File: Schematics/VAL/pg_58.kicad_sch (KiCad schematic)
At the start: 16 parts, among them U6001 F194, U6002 F194, U6003 F194, U6004 F194, U6005 F194, U6006 F194, U6007 F04, U6008 F138, U6009 F138, U6010 F37, U6011 F37, U6012 F240, U6013 F08, U6014 F00, U6015 F00, U6016 F00

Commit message: Align to grid
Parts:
- removed U6001, U6002, U6003, U6004, U6005, U6006: F194, symbol r1000:F194
- removed U6007: F04, symbol r1000:F04
- removed U6008, U6009: F138, symbol r1000:F138
- removed U6010, U6011: F37, symbol r1000:F37
- removed U6012: F240, symbol r1000:F240
- removed U6013: F08, symbol r1000:F08
- removed U6014, U6015, U6016: F00, symbol r1000:F00
- added U (x2): (no value), symbol r1000:F138
- added U (x3): (no value), symbol r1000:F00
- added U (x6): (no value), symbol r1000:F194
- added U: (no value), symbol r1000:F08
- added U (x2): (no value), symbol r1000:F37
- added U: (no value), symbol r1000:F240
- added U: (no value), symbol r1000:F04
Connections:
- net ALU_RAND0: now also U.3 (Q)
- net ALU_RAND1: now also U.3 (Q)
- net ALU_RAND2: now also U.3 (Q)
- net COND_TO_FIU~: now also U.1 (D0), U.12 (Y3_)
- net COUNT_ZEROS~: now also U.10 (Y5_)
- net C_MUX.SEL0: now also U.15 (Q0)
- net C_MUX.SEL1: now also U.1 (D0), U.14 (Q1)
- net C_MUX.SEL1.B0: now also U.3 (Q)
- net C_MUX.SEL1.B1: now also U.3 (Q)
- net DEC_LOOP~: now also U.13 (Y2_)
- net DIAG.D10: now also U.14 (Y2)
- net DIAG.D11: now also U.12 (Y3), U.2 (RSI)
- net DIAG.D12: now also U.2 (RSI), U.9 (Y4)
- net DIAG.D8: now also U.18 (Y0)
- net DIAG.D9: now also U.16 (Y1)
- net DIVIDE~: now also U.12 (Y3_)
- net FORCE_PASS_A~: now also U.1 (CLR), U.1 (CLR), U.1 (CLR), U.1 (D0), U.2 (D1)
- net FRAME~3: now also U.4 (I1)
- net GET_LIT~: now also U.2 (D1), U.9 (Y6_)
- net INC_LOOP~: now also U.14 (Y1_)
- net PD: now also U.4 (D1), U.5 (D2), U.5 (D2)
- net PROD_LEFT_16~: now also U.10 (Y5_)
- net PROD_LEFT_32~: now also U.9 (Y6_)
- net PU: now also U.1 (CLR), U.1 (CLR), U.1 (CLR), U.13 (I5), U.15 (I6), U.17 (I7), U.6 (D0), U.9 (S0), U.9 (S0), U.9 (S0), U.9 (S0), U.9 (S0), U.9 (S0)
- net SCAN_UIR~: now also U.1 (OE0), U.19 (OE1)
- net SNEAK.EN~: now also U.3 (Q)
- net SPLIT_C_SRC~: now also U.11 (Y4_)
- net START_MULT~: now also U.11 (Y4_)
- net UIR.ALU_FUNC0: now also U.13 (Q2)
- net UIR.ALU_FUNC1: now also U.12 (Q3), U.2 (RSI)
- net UIR.ALU_FUNC2: now also U.15 (Q0)
- net UIR.ALU_FUNC3: now also U.14 (Q1)
- net UIR.ALU_FUNC4: now also U.13 (Q2)
- net UIR.B~1: now also U.2 (I0)
- net UIR.C0: now also U.15 (Q0)
- net UIR.C1: now also U.14 (Q1)
- net UIR.C2: now also U.13 (Q2)
- net UIR.C3: now also U.12 (Q3), U.2 (RSI)
- net UIR.C4: now also U.15 (Q0)
- net UIR.C5: now also U.14 (Q1)
- net UIR.C_SOURCE: now also U.11 (I4), U.12 (Q3)
- net UIR.FRAME4: now also U.2 (RSI)
- net UIR.M_A_SRC0: now also U.13 (Q2)
- net UIR.M_A_SRC1: now also U.12 (Q3), U.8 (I3)
- net UIR.M_B_SRC0: now also U.15 (Q0)
- net UIR.M_B_SRC1: now also U.14 (Q1)
- net UIR.P: now also U.13 (Q2), U.2 (RSI)
- net UIR.RAND0: now also U.1 (D0), U.15 (Q0), U.2 (D1), U.2 (D1), U.4 (D1), U.6 (D0)
- net UIR.RAND1: now also U.1 (D0), U.14 (Q1), U.3 (S0), U.3 (S0)
- net UIR.RAND2: now also U.1 (D0), U.13 (Q2), U.2 (S1), U.2 (S1)
- net UIR.RAND3: now also U.1 (S2), U.1 (S2), U.12 (Q3), U.2 (D1), U.6 (I2)
- net UIR.SEL0: now also U.10 (S1), U.10 (S1), U.10 (S1), U.10 (S1), U.10 (S1), U.10 (S1)
- net UIR~.SCLK.B1: now also U.11 (CLK), U.11 (CLK), U.11 (CLK), U.11 (CLK)
- net UIR~.SCLK.B2: now also U.11 (CLK), U.11 (CLK)
- net WCS.D17: now also U.3 (D0)
- net WCS.D18: now also U.4 (D1)
- net WCS.D19: now also U.3 (D0)
- net WCS.D20: now also U.4 (D1)
- net WCS.D21: now also U.5 (D2)
- net WCS.D22: now also U.6 (D3)
- net WCS.D23: now also U.3 (D0)
- net WCS.D24: now also U.4 (D1)
- net WCS.D25: now also U.5 (D2)
- net WCS.D26: now also U.6 (D3)
- net WCS.D27: now also U.3 (D0)
- net WCS.D28: now also U.4 (D1)
- net WCS.D29: now also U.5 (D2)
- net WCS.D30: now also U.6 (D3)
- net WCS.D31: now also U.3 (D0)
- net WCS.D32: now also U.4 (D1)
- net WCS.D33: now also U.5 (D2)
- net WCS.D34: now also U.6 (D3)
- net WCS.D35: now also U.3 (D0)
- net WCS.D36: now also U.4 (D1)
- net WCS.D37: now also U.5 (D2)
- net WCS.D38: now also U.6 (D3)
- net WCS.P: now also U.5 (D2)
- new net: U.1 (D0), U.2 (D1), U.2 (Q)

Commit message: VAL: dedup, clock, dfsm
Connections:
- net UIR~.SCLK.B2 is gone; now on net UIR~.SCLK: U.11 (CLK), U.11 (CLK)
- net UIR~.SCLK.B1 renamed UIR~.SCLK
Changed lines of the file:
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@@
     )
   )
-  (global_label "UIR~.SCLK.B1" (shape input) (at 55.88 27.94 180) (fields_autoplaced)
+  (global_label "UIR~.SCLK" (shape input) (at 55.88 27.94 180) (fields_autoplaced)
     (effects (font (size 2.54 2.54)) (justify right))
     (property "Intersheet References" "${INTERSHEET_REFS}" (id 0) (at 25.8959 27.7813 0)
@@
     )
   )
-  (global_label "UIR~.SCLK.B2" (shape input) (at 309.88 22.86 180) (fields_autoplaced)
+  (global_label "UIR~.SCLK" (shape input) (at 309.88 22.86 180) (fields_autoplaced)
     (effects (font (size 2.54 2.54)) (justify right))
     (property "Intersheet References" "${INTERSHEET_REFS}" (id 0) (at 279.8959 22.7013 0)

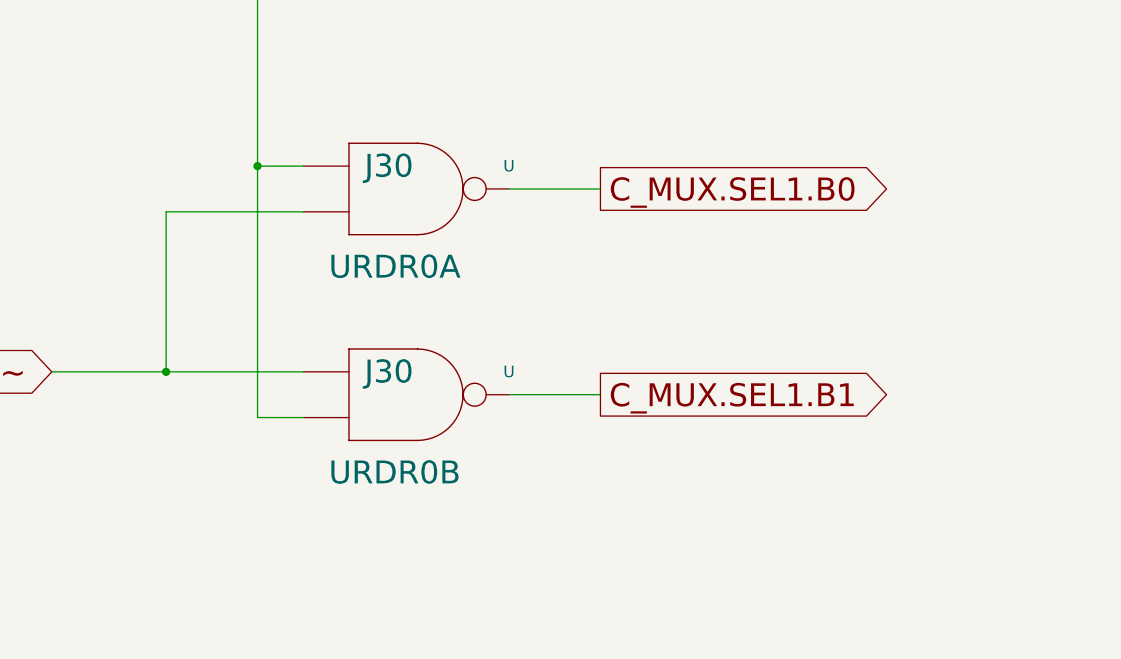
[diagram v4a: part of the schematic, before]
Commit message: VAL & SEQ: tested to 6.0 seconds (rm021)
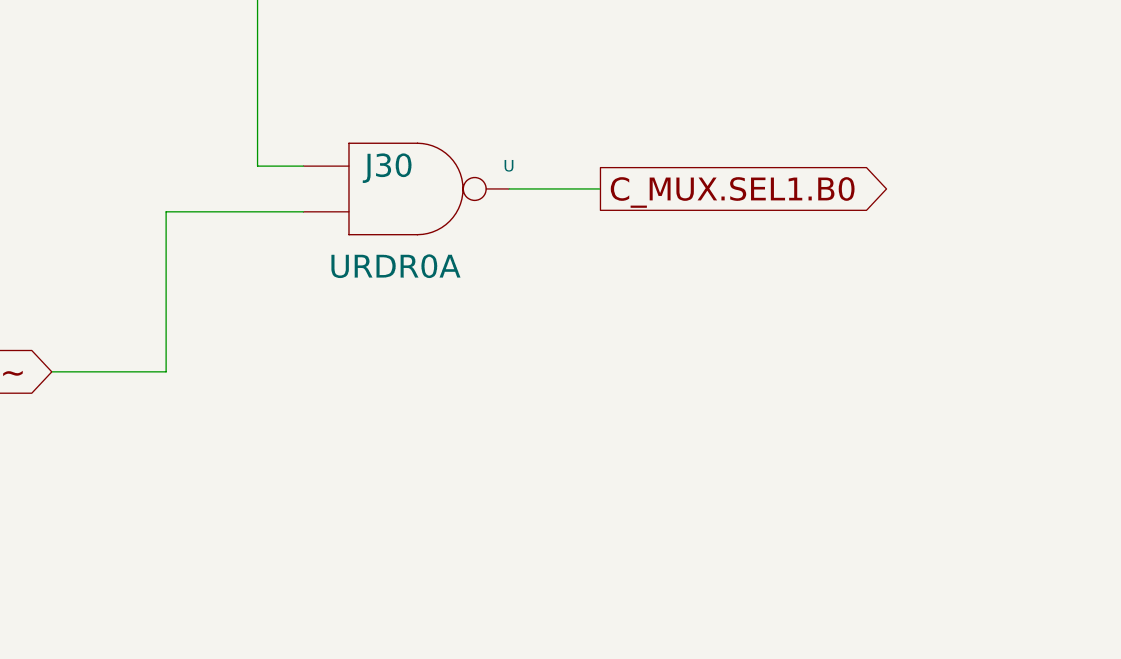
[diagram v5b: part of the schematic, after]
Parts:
- removed U: (no value), symbol r1000:F37
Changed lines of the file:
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@@
   (junction (at 325.12 109.22) (diameter 0) (color 0 0 0 0)
   )
-  (junction (at 208.28 91.44) (diameter 0) (color 0 0 0 0)
-  )
   (junction (at 490.22 208.28) (diameter 0) (color 0 0 0 0)
   )
@@
   )
   (junction (at 15.24 134.62) (diameter 0) (color 0 0 0 0)
-  )
-  (junction (at 198.12 114.3) (diameter 0) (color 0 0 0 0)
   )
   (junction (at 175.26 220.98) (diameter 0) (color 0 0 0 0)
@@
     (stroke (width 0) (type default))
   )
-  (wire (pts (xy 208.28 91.44) (xy 208.28 119.38))
-    (stroke (width 0) (type default))
-  )
   (wire (pts (xy 91.44 129.54) (xy 91.44 139.7))
     (stroke (width 0) (type default))
@@
     (stroke (width 0) (type default))
   )
-  (wire (pts (xy 236.22 116.84) (xy 246.38 116.84))
-    (stroke (width 0) (type default))
-  )
   (bus (pts (xy 25.4 81.28) (xy 25.4 157.48))
     (stroke (width 0) (type default))
@@
     (stroke (width 0) (type default))
   )
-  (wire (pts (xy 208.28 119.38) (xy 213.36 119.38))
-    (stroke (width 0) (type default))
-  )
   (wire (pts (xy 342.9 73.66) (xy 381 73.66))
     (stroke (width 0) (type default))
@@
   )
   (bus (pts (xy 25.4 238.76) (xy 25.4 243.84))
-    (stroke (width 0) (type default))
-  )
-  (wire (pts (xy 198.12 114.3) (xy 213.36 114.3))
     (stroke (width 0) (type default))
   )
@@
     (effects (font (size 2.54 2.54)) (justify left))
     (property "Intersheet References" "${INTERSHEET_REFS}" (id 0) (at 262.0917 164.9413 0)
-      (effects (font (size 1.905 1.905)) (justify left))
-    )
-  )
-  (global_label "C_MUX.SEL1.B1" (shape output) (at 246.38 116.84 0) (fields_autoplaced)
-    (effects (font (size 2.54 2.54)) (justify left))
-    (property "Intersheet References" "${INTERSHEET_REFS}" (id 0) (at 280.2346 116.6813 0)
       (effects (font (size 1.905 1.905)) (justify left))
     )
@@
     (pin "9")
   )
-  (symbol (lib_id "r1000:F37") (at 220.98 114.3 0) (unit 1)
-    (in_bom yes) (on_board yes)
-    (default_instance (reference "U") (unit 1) (value "") (footprint ""))
-    (property "Reference" "U" (id 0) (at 236.22 114.3 0)
-      (effects (font (size 1.27 1.27)))
-    )
-    (property "Value" "" (id 1) (at 222.885 119.38 0)
-      (effects (font (size 2.54 2.54)))
-    )
-    (property "Footprint" "" (id 2) (at 220.98 101.6 0)
-      (effects (font (size 1.27 1.27)) hide)
-    )
-    (property "Datasheet" "" (id 3) (at 220.98 101.6 0)
-      (effects (font (size 1.27 1.27)) hide)
-    )
-    (property "Location" "J30" (id 4) (at 222.885 114.3 0)
-      (effects (font (size 2.54 2.54)))
-    )
-    (property "Name" "URDR0B" (id 5) (at 223.52 127 0)
-      (effects (font (size 2.54 2.54)) (justify bottom))
-    )
-    (pin "1")
-    (pin "2")
-    (pin "3")
-  )
   (symbol (lib_id "r1000:F240") (at 233.68 327.66 0) (unit 1)

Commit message: Tested to 12.05s (rc016)
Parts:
- removed U (x4): (no value), symbol r1000:F194
- added U (x2): XSR8, symbol r1000:XSR8
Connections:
- net DIAG.D11: now also U.3 (RSI)
- net DIAG.D12: now also U.3 (RSI)
- net FORCE_PASS_A~: now also U.2 (CLR)
- net PU: now also U.5 (S0), U.5 (S0)
- net UIR.ALU_FUNC0: now also U.17 (Q2)
- net UIR.ALU_FUNC1: now also U.18 (Q3)
- net UIR.ALU_FUNC2: now also U.19 (Q4)
- net UIR.ALU_FUNC3: now also U.20 (Q5)
- net UIR.ALU_FUNC4: now also U.21 (Q6)
- net UIR.C0: now also U.15 (Q0)
- net UIR.C1: now also U.16 (Q1)
- net UIR.C2: now also U.17 (Q2)
- net UIR.C3: now also U.18 (Q3)
- net UIR.C4: now also U.19 (Q4)
- net UIR.C5: now also U.20 (Q5)
- net UIR.C_SOURCE: now also U.22 (Q7)
- net UIR.M_A_SRC0: now also U.21 (Q6)
- net UIR.M_A_SRC1: now also U.22 (Q7)
- net UIR.M_B_SRC0: now also U.15 (Q0)
- net UIR.M_B_SRC1: now also U.16 (Q1)
- net UIR.SEL0: now also U.6 (S1), U.6 (S1)
- net UIR~.SCLK: now also U.1 (CLK), U.1 (CLK)
- net WCS.D23: now also U.7 (D0)
- net WCS.D24: now also U.8 (D1)
- net WCS.D25: now also U.9 (D2)
- net WCS.D26: now also U.10 (D3)
- net WCS.D27: now also U.11 (D4)
- net WCS.D28: now also U.12 (D5)
- net WCS.D29: now also U.13 (D6)
- net WCS.D30: now also U.14 (D7)
- net WCS.D31: now also U.7 (D0)
- net WCS.D32: now also U.8 (D1)
- net WCS.D33: now also U.9 (D2)
- net WCS.D34: now also U.10 (D3)
- net WCS.D35: now also U.11 (D4)
- net WCS.D36: now also U.12 (D5)
- net WCS.D37: now also U.13 (D6)
- net WCS.D38: now also U.14 (D7)
- no-connect marks 17 -> 16
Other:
- moved on the sheet: U

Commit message: VAL tested to 18.5 seconds (rm082)
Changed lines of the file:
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@@
   (junction (at 370.84 284.48) (diameter 0) (color 0 0 0 0)
   )
-  (junction (at 10.16 114.3) (diameter 0) (color 0 0 0 0)
-  )
   (junction (at 490.22 231.14) (diameter 0) (color 0 0 0 0)
   )
@@
   )
   (junction (at 175.26 220.98) (diameter 0) (color 0 0 0 0)
-  )
-  (junction (at 15.24 50.8) (diameter 0) (color 0 0 0 0)
   )
   (no_connect (at 391.16 327.66))
@@
     (stroke (width 0) (type default))
   )
-  (wire (pts (xy 83.82 139.7) (xy 83.82 134.62))
-    (stroke (width 0) (type default))
-  )
-  (wire (pts (xy 55.88 27.94) (xy 58.42 27.94))
+  (wire (pts (xy 83.82 139.7) (xy 83.82 137.16))
+    (stroke (width 0) (type default))
+  )
+  (wire (pts (xy 73.66 15.24) (xy 86.36 15.24))
     (stroke (width 0) (type default))
   )
@@
     (stroke (width 0) (type default))
   )
-  (wire (pts (xy 15.24 33.02) (xy 15.24 50.8))
-    (stroke (width 0) (type default))
-  )
   (wire (pts (xy 342.9 76.2) (xy 381 76.2))
     (stroke (width 0) (type default))
@@
     (stroke (width 0) (type default))
   )
-  (wire (pts (xy 91.44 129.54) (xy 91.44 139.7))
+  (wire (pts (xy 91.44 132.08) (xy 91.44 139.7))
     (stroke (width 0) (type default))
   )
@@
     (stroke (width 0) (type default))
   )
-  (wire (pts (xy 58.42 27.94) (xy 58.42 33.02))
-    (stroke (width 0) (type default))
-  )
-  (wire (pts (xy 45.72 129.54) (xy 91.44 129.54))
+  (wire (pts (xy 60.96 132.08) (xy 91.44 132.08))
     (stroke (width 0) (type default))
   )
@@
     (stroke (width 0) (type default))
   )
-  (wire (pts (xy 15.24 50.8) (xy 83.82 50.8))
+  (wire (pts (xy 63.5 55.88) (xy 83.82 55.88))
     (stroke (width 0) (type default))
   )
@@
     (stroke (width 0) (type default))
   )
-  (wire (pts (xy 15.24 50.8) (xy 15.24 134.62))
-    (stroke (width 0) (type default))
-  )
   (wire (pts (xy 152.4 162.56) (xy 182.88 162.56))
     (stroke (width 0) (type default))
@@
     (stroke (width 0) (type default))
   )
-  (wire (pts (xy 58.42 33.02) (xy 15.24 33.02))
-    (stroke (width 0) (type default))
-  )
   (wire (pts (xy 490.22 231.14) (xy 490.22 208.28))
     (stroke (width 0) (type default))
@@
     (stroke (width 0) (type default))
   )
-  (wire (pts (xy 10.16 195.58) (xy 10.16 114.3))
-    (stroke (width 0) (type default))
-  )
   (bus (pts (xy 340.36 83.82) (xy 340.36 88.9))
     (stroke (width 0) (type default))
@@
     (stroke (width 0) (type default))
   )
-  (wire (pts (xy 83.82 58.42) (xy 83.82 50.8))
+  (wire (pts (xy 83.82 58.42) (xy 83.82 55.88))
     (stroke (width 0) (type default))
   )
@@
     (stroke (width 0) (type default))
   )
-  (wire (pts (xy 78.74 10.16) (xy 78.74 15.24))
-    (stroke (width 0) (type default))
-  )
   (bus (pts (xy 340.36 78.74) (xy 340.36 83.82))
     (stroke (width 0) (type default))
@@
     (stroke (width 0) (type default))
   )
-  (wire (pts (xy 10.16 195.58) (xy 71.12 195.58))
+  (wire (pts (xy 48.26 195.58) (xy 71.12 195.58))
     (stroke (width 0) (type default))
   )
@@
     (stroke (width 0) (type default))
   )
-  (wire (pts (xy 15.24 134.62) (xy 83.82 134.62))
+  (wire (pts (xy 63.5 137.16) (xy 83.82 137.16))
     (stroke (width 0) (type default))
   )
@@
     (stroke (width 0) (type default))
   )
-  (wire (pts (xy 10.16 15.24) (xy 78.74 15.24))
-    (stroke (width 0) (type default))
-  )
-  (wire (pts (xy 10.16 114.3) (xy 10.16 15.24))
-    (stroke (width 0) (type default))
-  )
   (wire (pts (xy 60.96 63.5) (xy 68.58 63.5))
     (stroke (width 0) (type default))
@@
     (stroke (width 0) (type default))
   )
-  (wire (pts (xy 73.66 10.16) (xy 78.74 10.16))
+  (wire (pts (xy 73.66 10.16) (xy 86.36 10.16))
     (stroke (width 0) (type default))
   )
@@
     (stroke (width 0) (type default))
   )
-  (wire (pts (xy 10.16 114.3) (xy 71.12 114.3))
+  (wire (pts (xy 48.26 114.3) (xy 71.12 114.3))
     (stroke (width 0) (type default))
   )
@@
     (effects (font (size 2.54 2.54)) (justify left bottom))
   )
+  (label "UIR~.SCLK" (at 63.5 137.16 0) (fields_autoplaced)
+    (effects (font (size 2.54 2.54)) (justify left bottom))
+  )
   (label "WCS.D18" (at 30.48 83.82 0) (fields_autoplaced)
     (effects (font (size 2.54 2.54)) (justify left bottom))
@@
     (effects (font (size 2.54 2.54)) (justify left bottom))
   )
+  (label "UIR.SEL0" (at 48.26 114.3 0) (fields_autoplaced)
+    (effects (font (size 2.54 2.54)) (justify left bottom))
+  )
   (label "UIR.M_A_SRC1" (at 325.12 317.5 0) (fields_autoplaced)
     (effects (font (size 2.54 2.54)) (justify left bottom))
   )
+  (label "UIR.SEL0" (at 48.26 195.58 0) (fields_autoplaced)
+    (effects (font (size 2.54 2.54)) (justify left bottom))
+  )
   (label "DIAG.D11" (at 396.24 317.5 0) (fields_autoplaced)
     (effects (font (size 2.54 2.54)) (justify left bottom))
@@
     (effects (font (size 2.54 2.54)) (justify left bottom))
   )
-  (label "FORCE_PASS_A~" (at 45.72 129.54 0) (fields_autoplaced)
+  (label "FORCE_PASS_A~" (at 60.96 132.08 0) (fields_autoplaced)
     (effects (font (size 2.54 2.54)) (justify left bottom))
   )
@@
   )
   (label "WCS.D36" (at 358.14 86.36 0) (fields_autoplaced)
+    (effects (font (size 2.54 2.54)) (justify left bottom))
+  )
+  (label "UIR~.SCLK" (at 63.5 55.88 0) (fields_autoplaced)
     (effects (font (size 2.54 2.54)) (justify left bottom))
   )
@@
     )
   )
-  (global_label "UIR~.SCLK" (shape input) (at 55.88 27.94 180) (fields_autoplaced)
+  (global_label "UIR~.SCLK" (shape input) (at 73.66 15.24 180) (fields_autoplaced)
     (effects (font (size 2.54 2.54)) (justify right))
-    (property "Intersheet References" "${INTERSHEET_REFS}" (id 0) (at 25.8959 27.7813 0)
+    (property "Intersheet References" "${INTERSHEET_REFS}" (id 0) (at 43.6759 15.0813 0)
       (effects (font (size 1.905 1.905)) (justify right))
     )
@@
     )
   )
-  (global_label "WCS.D[17..38]" (shape input) (at 246.38 43.18 180) (fields_autoplaced)
+  (global_label "WCS.D[0..38]" (shape input) (at 246.38 43.18 180) (fields_autoplaced)
     (effects (font (size 2.54 2.54)) (justify right))
-    (property "Intersheet References" "${INTERSHEET_REFS}" (id 0) (at 214.4607 43.0213 0)
+    (property "Intersheet References" "${INTERSHEET_REFS}" (id 0) (at 216.2131 43.18 0)
       (effects (font (size 1.905 1.905)) (justify right))
     )
@@
     )
   )
-  (global_label "DIAG.D[8..12]" (shape output) (at 424.18 325.12 0) (fields_autoplaced)
-    (effects (font (size 2.54 2.54)) (justify left))
-    (property "Intersheet References" "${INTERSHEET_REFS}" (id 0) (at 454.285 324.9613 0)
-      (effects (font (size 1.905 1.905)) (justify left))
-    )
+  (global_label "DIAG.D[0..15]" (shape output) (at 424.18 325.12 0) (fields_autoplaced)
+    (effects (font (size 2.54 2.54)) (justify left))
+    (property "Intersheet References" "${INTERSHEET_REFS}" (id 0) (at 454.9516 325.12 0)
+      (effects (font (size 1.905 1.905)) (justify left))
+    )

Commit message: VAL: prune DFSM
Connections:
- removed net FORCE_PASS_A~: U.1 (CLR), U.2 (CLR), U.2 (D1)
- no-connect marks 16 -> 19
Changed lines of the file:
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@@
   (no_connect (at 228.6 208.28))
   (no_connect (at 391.16 332.74))
+  (no_connect (at 401.32 38.1))
+  (no_connect (at 91.44 139.7))
+  (no_connect (at 213.36 96.52))
   (no_connect (at 71.12 180.34))
   (no_connect (at 228.6 190.5))
@@
     (stroke (width 0) (type default))
   )
-  (wire (pts (xy 401.32 35.56) (xy 401.32 38.1))
-    (stroke (width 0) (type default))
-  )
   (bus (pts (xy 340.36 63.5) (xy 340.36 68.58))
     (stroke (width 0) (type default))
@@
     (stroke (width 0) (type default))
   )
-  (wire (pts (xy 213.36 96.52) (xy 198.12 96.52))
-    (stroke (width 0) (type default))
-  )
   (wire (pts (xy 60.96 88.9) (xy 71.12 88.9))
     (stroke (width 0) (type default))
@@
     (stroke (width 0) (type default))
   )
-  (wire (pts (xy 91.44 132.08) (xy 91.44 139.7))
-    (stroke (width 0) (type default))
-  )
   (wire (pts (xy 391.16 312.42) (xy 419.1 312.42))
     (stroke (width 0) (type default))
@@
     (stroke (width 0) (type default))
   )
-  (wire (pts (xy 60.96 132.08) (xy 91.44 132.08))
-    (stroke (width 0) (type default))
-  )
   (wire (pts (xy 175.26 220.98) (xy 182.88 220.98))
     (stroke (width 0) (type default))
@@
     (stroke (width 0) (type default))
   )
-  (wire (pts (xy 185.42 114.3) (xy 198.12 114.3))
-    (stroke (width 0) (type default))
-  )
   (bus (pts (xy 25.4 297.18) (xy 25.4 302.26))
     (stroke (width 0) (type default))
@@
     (stroke (width 0) (type default))
   )
-  (wire (pts (xy 431.8 35.56) (xy 401.32 35.56))
-    (stroke (width 0) (type default))
-  )
   (wire (pts (xy 518.16 251.46) (xy 523.24 251.46))
     (stroke (width 0) (type default))
@@
     (stroke (width 0) (type default))
   )
-  (wire (pts (xy 198.12 96.52) (xy 198.12 114.3))
-    (stroke (width 0) (type default))
-  )
   (wire (pts (xy 83.82 243.84) (xy 83.82 246.38))
     (stroke (width 0) (type default))
@@
     (effects (font (size 2.54 2.54)) (justify left bottom))
   )
-  (label "FORCE_PASS_A~" (at 60.96 132.08 0) (fields_autoplaced)
-    (effects (font (size 2.54 2.54)) (justify left bottom))
-  )
   (label "WCS.D25" (at 48.26 279.4 0) (fields_autoplaced)
     (effects (font (size 2.54 2.54)) (justify left bottom))
@@
   )
   (label "UIR.RAND2" (at 152.4 238.76 0) (fields_autoplaced)
-    (effects (font (size 2.54 2.54)) (justify left bottom))
-  )
-  (label "FORCE_PASS_A~" (at 401.32 35.56 0) (fields_autoplaced)
     (effects (font (size 2.54 2.54)) (justify left bottom))
   )
@@
     )
   )
-  (global_label "FORCE_PASS_A~" (shape input) (at 185.42 114.3 180) (fields_autoplaced)
-    (effects (font (size 2.54 2.54)) (justify right))
-    (property "Intersheet References" "${INTERSHEET_REFS}" (id 0) (at 150.9607 114.1413 0)
-      (effects (font (size 1.905 1.905)) (justify right))
-    )
-  )
